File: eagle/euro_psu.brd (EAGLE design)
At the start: 99.4 x 50.2 mm, 40 parts, among them U1 POWER

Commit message: silkscreen draft
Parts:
- removed IC2: (no value), v-reg:317TS
- added LM317-2: (no value), v-reg:317TS
- added U2: POWER, eurorack:POWER_16
- moved PHASE1 17.8 mm to (21.6, 47.0)
- moved CT 13.7 mm to (16.5, 47.0)
- moved PHASE2 12.7 mm to (11.4, 47.0)
- moved U1 4.49 mm to (54.6, 44.5)
- moved C10 2.54 mm to (8.89, 11.4)
- moved C11 2.54 mm to (8.89, 29.2)
- moved C2 2.54 mm to (44.5, 11.4)
- moved C4 2.54 mm to (44.5, 29.2)
- moved C5 1.27 mm to (54.6, 3.81)
- moved D1 1.27 mm to (30.5, 43.2)
- moved D3 1.27 mm to (30.5, 38.1)
- moved C9 0.64 mm to (89.5, 27.9)
- renumbered +5_ADJ1 to +5_ADJ, -12_ADJ1 to -12_ADJ, IC1 to LM317-1, IC3 to LM337, LED1 to LED-12, LED2 to LED12, LED3 to LED5
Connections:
- net GNDA: now also U2.3, U2.4, U2.5, U2.6, U2.7, U2.8
- net N$10: now also U2.1, U2.2
- net N$11: now also LM317-2.2, U2.10, U2.9; no longer IC2.2
- net N$12: now also U2.11, U2.12
- net N$4: now also LM317-2.3; no longer IC2.3
- net N$6: now also LM317-2.1; no longer IC2.1
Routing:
- net N$12: track 51.9 -> 93.7 mm, vias 0 -> 1
- net N$11: track 138.9 -> 116.5 mm
- net N$1: track 39.7 -> 22.0 mm
- net GNDA: track 290.9 -> 307.9 mm
- net N$4: track 178.7 -> 186.2 mm, vias 1 -> 0
- net N$10: track 62.0 -> 56.9 mm, vias 1 -> 0
- net N$3: track 117.5 -> 121.6 mm
- net N$6: track 22.8 -> 25.8 mm
- net N$2: track 12.0 -> 10.4 mm
- net N$8: track 25.1 -> 24.2 mm
- net N$25: track 15.1 -> 14.5 mm
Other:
- board text added: "https://github.com/jbeuckm/euro_psu"
- board text removed: "https://github.com/jbeuckm/Roland-121-VCF"

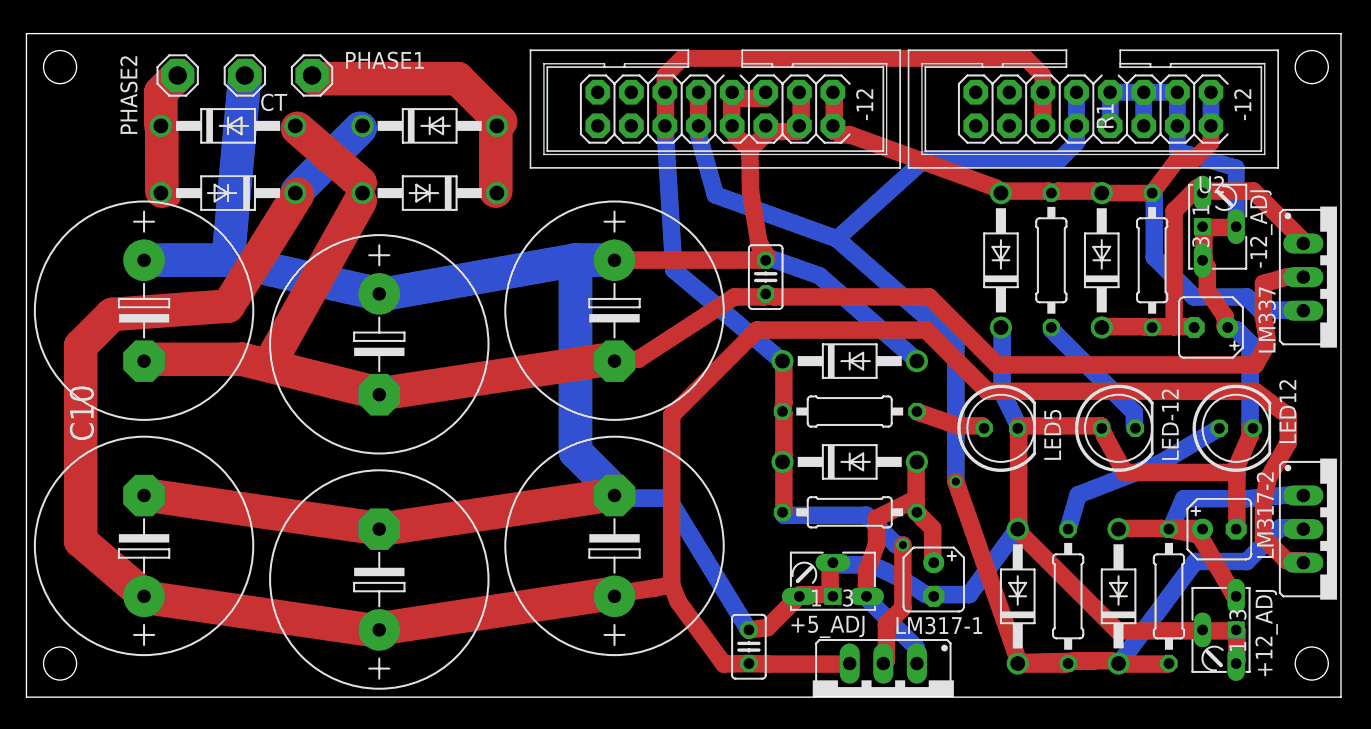
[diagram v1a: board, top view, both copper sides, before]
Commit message: rerouted with regulator protection diodes
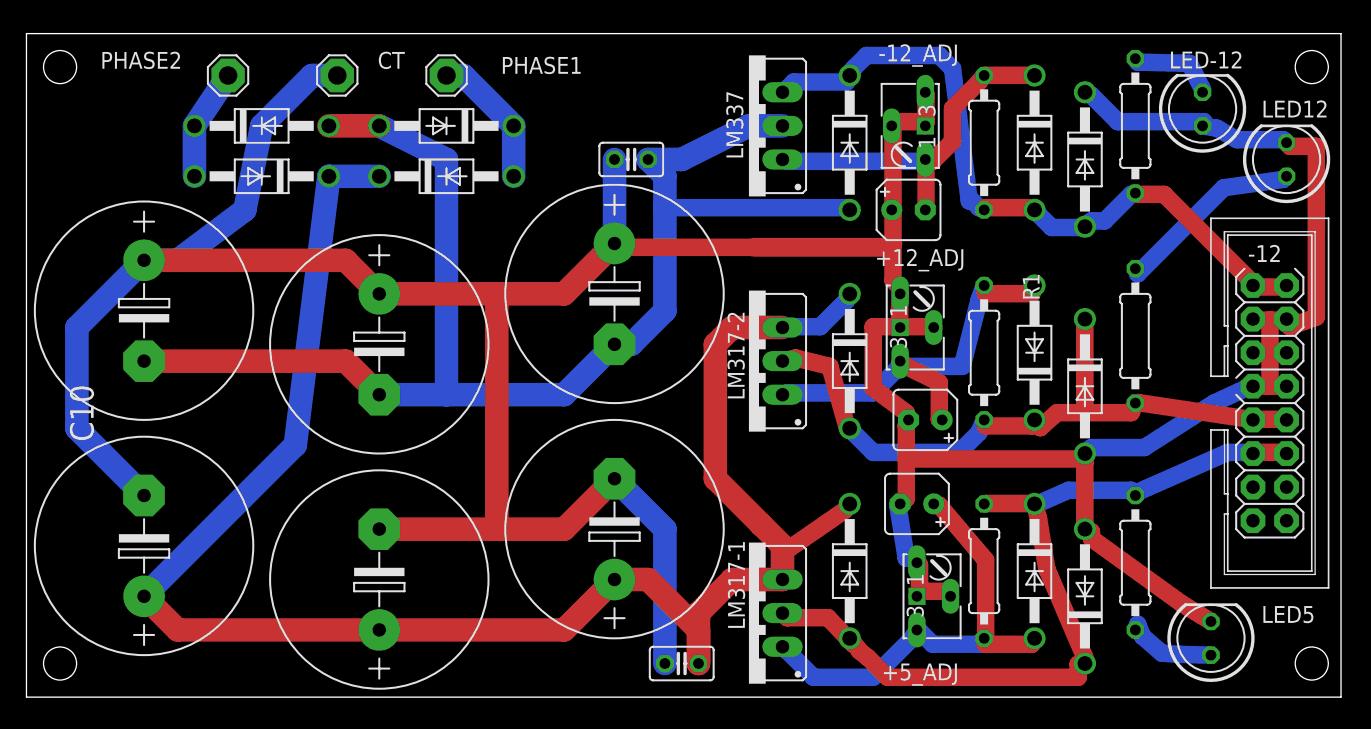
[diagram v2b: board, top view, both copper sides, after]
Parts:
- removed U2: POWER, eurorack:POWER_16
- added D11, D12, D13: 1N4004, diode:DO41-10
- R5, R6: value 4k7 -> 10k
- moved LM317-2 46.2 mm to (54.6, 25.4), turned to 90 degrees
- moved LM337 45.9 mm to (54.6, 43.2), turned to 90 degrees
- moved U1 44.0 mm to (94.0, 24.8), turned to 270 degrees
- moved +12_ADJ 34.2 mm to (66.0, 27.9), turned to 90 degrees
- moved D8 25.1 mm to (80.0, 7.62), turned to 90 degrees
- moved LED-12 25.0 mm to (88.9, 44.5), turned to 90 degrees
- moved C9 24.5 mm to (66.7, 36.8), turned to 0 degrees
- moved R4 24.4 mm to (83.8, 10.2), turned to 90 degrees
- moved C7 23.7 mm to (67.9, 21.0), turned to 180 degrees
- moved R2 23.1 mm to (72.4, 26.0)
- moved LED5 22.5 mm to (89.5, 4.45), turned to 90 degrees
- moved -12_ADJ 22.3 mm to (67.9, 43.2), turned to 270 degrees
- moved LED12 20.7 mm to (95.2, 40.6), turned to 90 degrees
- moved R5 20.3 mm to (83.8, 27.3)
- moved D6 19.5 mm to (76.2, 26.0)
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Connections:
- net GNDA: no longer U2.3, U2.4, U2.5, U2.6, U2.7, U2.8
- net N$10: now also D13.C; no longer U2.1, U2.2
- net N$11: now also D12.A; no longer U2.10, U2.9
- net N$12: now also D11.A; no longer U2.11, U2.12
- net N$3: now also D13.A
- net N$4: now also D11.C, D12.C
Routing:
- net N$11: track 116.5 -> 52.8 mm, vias 1 -> 0
- net N$4: track 186.2 -> 140.9 mm
- net N$12: track 93.7 -> 63.8 mm, vias 1 -> 0
- net N$3: track 121.6 -> 107.1 mm
- net N$1: track 22.0 -> 10.5 mm
- net N$8: track 24.2 -> 35.1 mm
- net N$6: track 25.8 -> 32.4 mm
- net N$24: track 10.2 -> 6.64 mm
- net N$10: track 56.9 -> 53.6 mm
- net N$2: track 10.4 -> 8.39 mm
- net N$21: track 5.36 -> 7.08 mm
- net N$5: track 28.3 -> 27.1 mm
- net GNDA: track 307.9 -> 307.2 mm

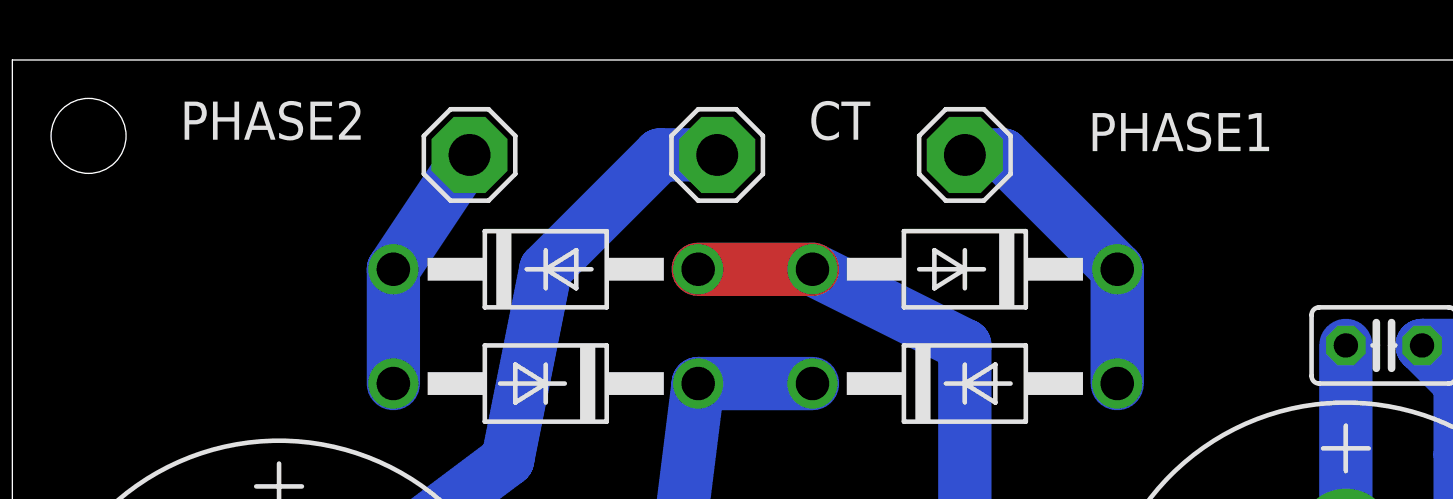
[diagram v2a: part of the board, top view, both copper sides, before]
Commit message: vector silkscreen
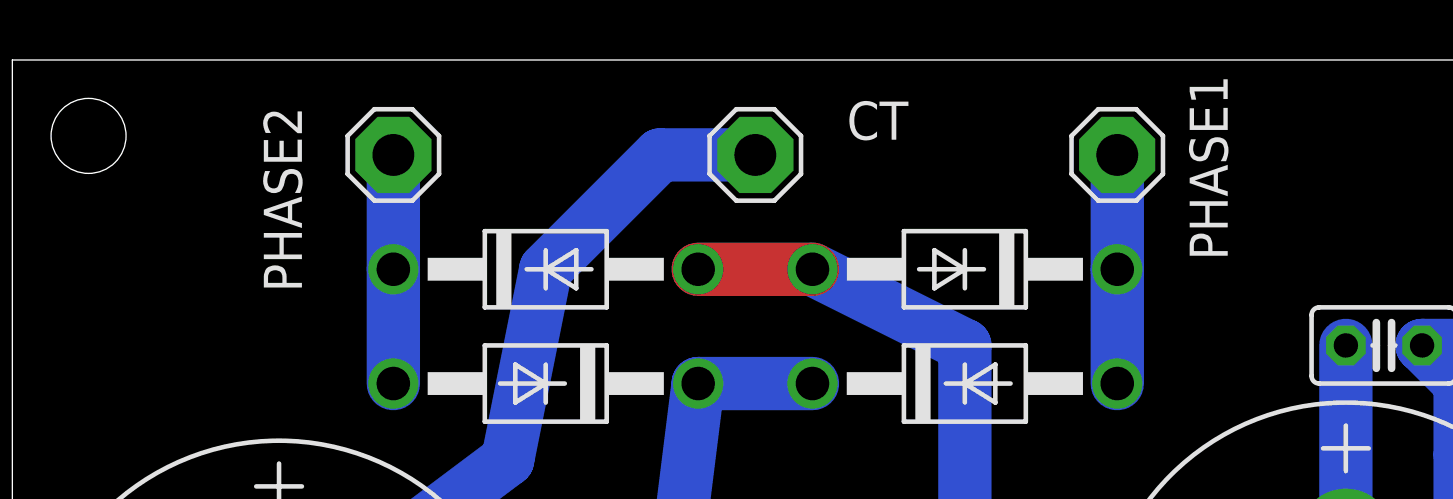
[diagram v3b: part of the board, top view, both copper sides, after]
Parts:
- moved PHASE1 5.08 mm to (36.8, 47.0)
- moved PHASE2 2.54 mm to (12.7, 47.0)
- moved CT 1.27 mm to (24.8, 47.0)
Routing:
- net N$1: track 10.5 -> 7.62 mm
- net GNDA: track 307.2 -> 308.5 mm
- net N$2: track 8.39 -> 7.62 mm
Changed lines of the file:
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@@
 <?xml version="1.0" encoding="utf-8"?>
 <!DOCTYPE eagle SYSTEM "eagle.dtd">
-<eagle version="7.6.0">
+<eagle version="8.3.2">
 <drawing>
 <settings>
 <setting alwaysvectorfont="no"/>
+<setting keepoldvectorfont="yes"/>
 <setting verticaltext="up"/>
 </settings>
@@
 <wire x1="99.365" y1="50.155" x2="0" y2="50.155" width="0" layer="20"/>
 <wire x1="0" y1="50.155" x2="0" y2="0" width="0" layer="20"/>
-<text x="53.975" y="19.05" size="2.1844" layer="26" rot="MR0">https://github.com/jbeuckm/euro_psu</text>
+<text x="59.055" y="17.78" size="2" layer="26" font="vector" rot="MR0">https://github.com/jbeuckm/euro_psu</text>
 <text x="52.07" y="22.225" size="2.1844" layer="26" rot="MR0">Release v0.1</text>
 <hole x="2.54" y="47.625" drill="2.5"/>
@@
 <element name="D3" library="diode" package="DO41-10" value="1N4004" x="31.75" y="43.18" smashed="yes" rot="R180"/>
 <element name="D4" library="diode" package="DO41-10" value="1N4004" x="17.78" y="43.18" smashed="yes"/>
-<element name="PHASE1" library="solpad" package="SE14" value="SE14" x="31.75" y="46.99" smashed="yes">
-<attribute name="NAME" x="42.037" y="48.387" size="1.27" layer="25" ratio="10" rot="R180"/>
-<attribute name="VALUE" x="31.75" y="47.371" size="0.0254" layer="27"/>
-</element>
-<element name="CT" library="solpad" package="SE14" value="SE14" x="23.495" y="46.99" smashed="yes">
-<attribute name="NAME" x="26.543" y="47.498" size="1.27" layer="25" ratio="10"/>
-<attribute name="VALUE" x="23.495" y="47.371" size="0.0254" layer="27"/>
-</element>
-<element name="PHASE2" library="solpad" package="SE14" value="SE14" x="15.24" y="46.99" smashed="yes">
-<attribute name="NAME" x="5.588" y="47.498" size="1.27" layer="25" ratio="10"/>
-<attribute name="VALUE" x="14.605" y="47.371" size="0.0254" layer="27"/>
+<element name="PHASE1" library="solpad" package="SE14" value="SE14" x="36.83" y="46.99" smashed="yes">
+<attribute name="NAME" x="39.243" y="49.657" size="1.27" layer="25" ratio="10" rot="R270"/>
+<attribute name="VALUE" x="36.83" y="47.371" size="0.0254" layer="27"/>
+</element>
+<element name="CT" library="solpad" package="SE14" value="SE14" x="24.765" y="46.99" smashed="yes">
+<attribute name="NAME" x="27.813" y="47.498" size="1.27" layer="25" ratio="10"/>
+<attribute name="VALUE" x="24.765" y="47.371" size="0.0254" layer="27"/>
+</element>
+<element name="PHASE2" library="solpad" package="SE14" value="SE14" x="12.7" y="46.99" smashed="yes">
+<attribute name="NAME" x="9.652" y="42.418" size="1.27" layer="25" ratio="10" rot="R90"/>
+<attribute name="VALUE" x="12.065" y="47.371" size="0.0254" layer="27"/>
 </element>
 <element name="C1" library="rcl" package="E7,5-16" value="3300uF" x="26.67" y="8.89" smashed="yes" rot="R90">
@@
 <contactref element="D1" pad="A"/>
 <contactref element="PHASE1" pad="MP"/>
-<wire x1="31.75" y1="46.99" x2="33.02" y2="46.99" width="1.778" layer="16"/>
 <wire x1="36.83" y1="43.18" x2="36.83" y2="39.37" width="1.778" layer="16"/>
-<wire x1="33.02" y1="46.99" x2="36.83" y2="43.18" width="1.778" layer="16"/>
+<wire x1="36.83" y1="46.99" x2="36.83" y2="43.18" width="1.778" layer="16"/>
 </signal>
 <signal name="N$2">
@@
 <contactref element="D4" pad="C"/>
 <contactref element="PHASE2" pad="MP"/>
-<wire x1="12.7" y1="43.18" x2="15.24" y2="46.99" width="1.778" layer="16"/>
+<wire x1="12.7" y1="43.18" x2="12.7" y2="46.99" width="1.778" layer="16"/>
 <wire x1="12.7" y1="43.18" x2="12.7" y2="39.37" width="1.778" layer="16"/>
 </signal>
@@
 <wire x1="16.51" y1="36.83" x2="17.78" y2="43.18" width="1.778" layer="16"/>
 <wire x1="17.78" y1="43.18" x2="21.59" y2="46.99" width="1.778" layer="16"/>
-<wire x1="21.59" y1="46.99" x2="23.495" y2="46.99" width="1.778" layer="16"/>
+<wire x1="21.59" y1="46.99" x2="24.765" y2="46.99" width="1.778" layer="16"/>
 <wire x1="8.89" y1="33.02" x2="24.13" y2="33.02" width="1.778" layer="1"/>
 <wire x1="24.13" y1="33.02" x2="26.67" y2="30.48" width="1.778" layer="1"/>

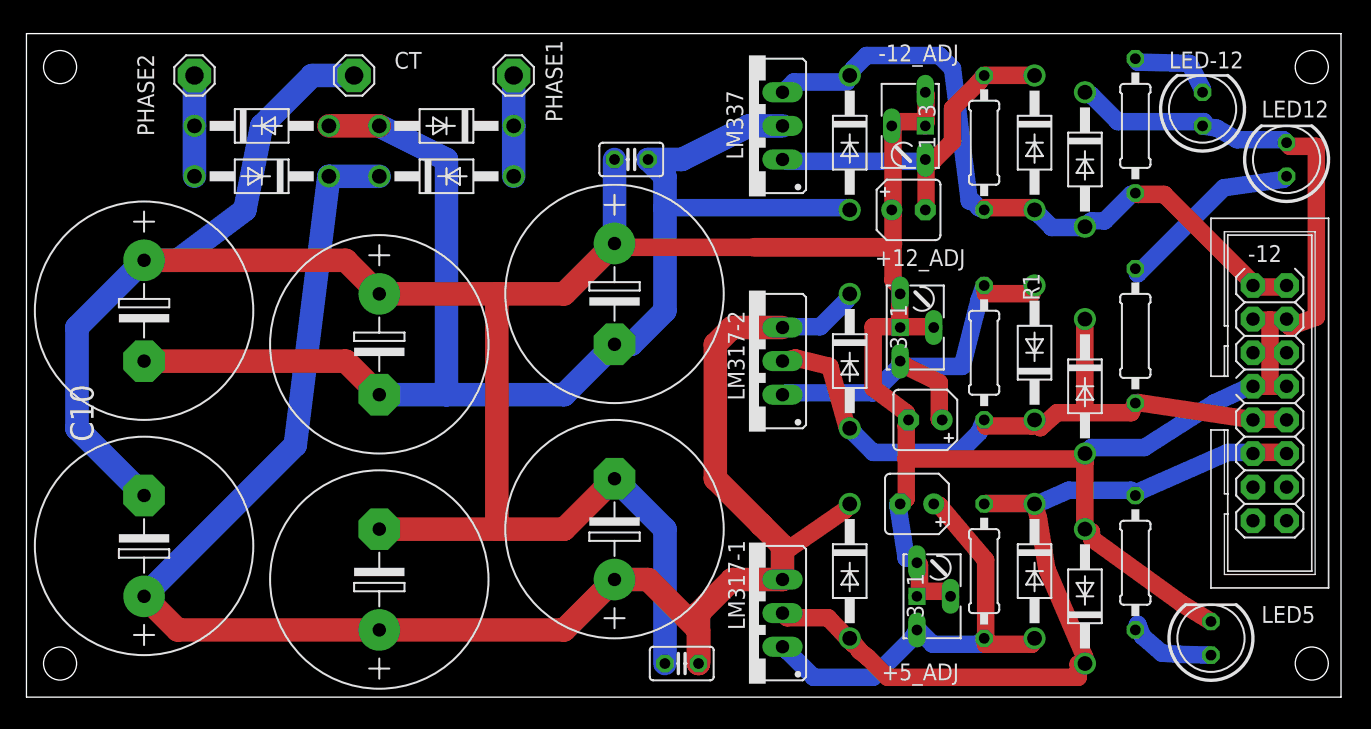
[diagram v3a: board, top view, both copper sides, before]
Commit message: tweaked for more space behind the regulators
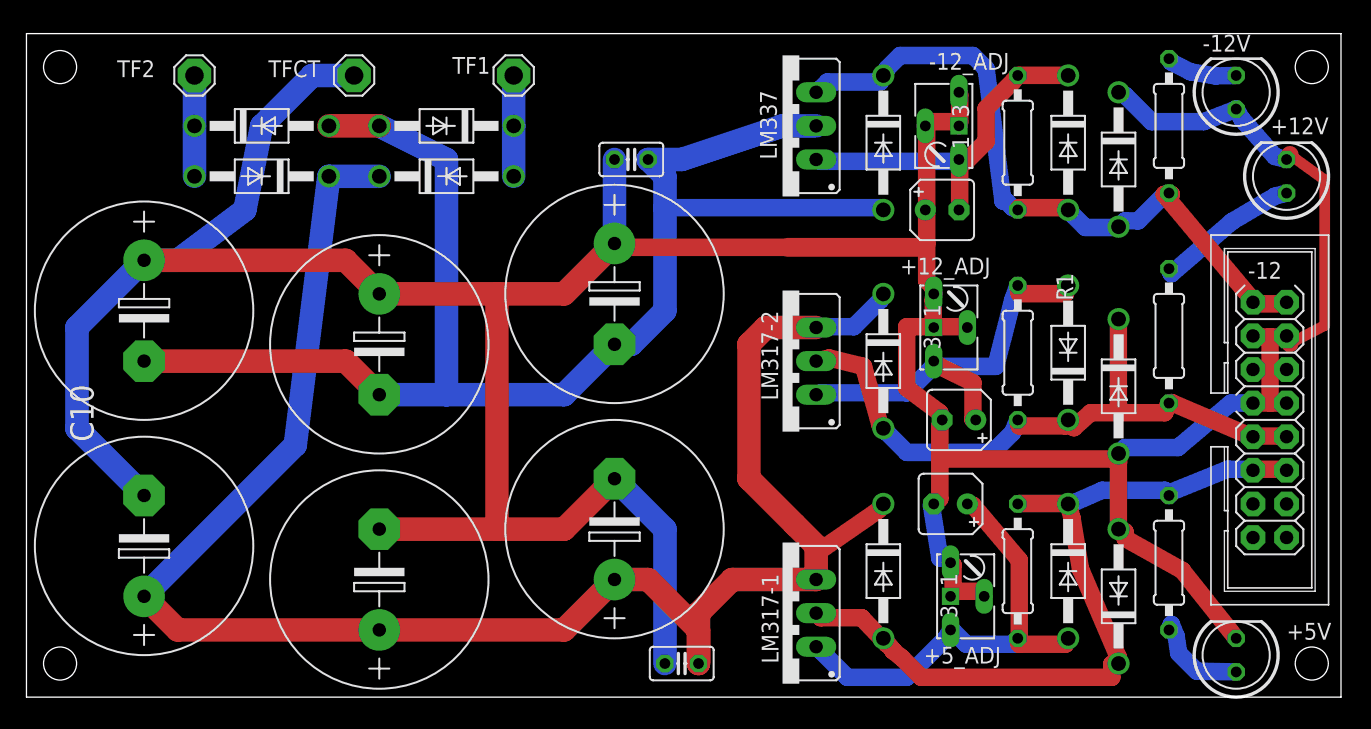
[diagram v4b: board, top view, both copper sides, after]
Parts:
- removed LED-12, LED12, LED5: (no value), led:LED5MM
- added +12V, +5V, -12V: (no value), led:LED5MM
- moved -12_ADJ 2.54 mm to (70.5, 43.2)
- moved C7 2.54 mm to (70.5, 21.0)
- moved C9 2.54 mm to (69.2, 36.8)
- moved R1 2.54 mm to (74.9, 41.9)
- moved R2 2.54 mm to (74.9, 26.0)
- moved R3 2.54 mm to (74.9, 9.53)
- moved R4 2.54 mm to (86.4, 10.2)
- moved R5 2.54 mm to (86.4, 27.3)
- moved R6 2.54 mm to (86.4, 43.2)
- moved D11 2.54 mm to (64.8, 9.53)
- moved D12 2.54 mm to (64.8, 25.4)
- moved D13 2.54 mm to (64.8, 41.9)
- moved LM317-1 2.54 mm to (57.1, 6.35)
- moved LM317-2 2.54 mm to (57.1, 25.4)
- moved LM337 2.54 mm to (57.1, 43.2)
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- renumbered CT to TFCT, PHASE1 to TF1, PHASE2 to TF2
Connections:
- net GNDA: now also +12V.K, +5V.K, -12V.A; no longer LED-12.A, LED12.K, LED5.K
- net N$21: now also +5V.A; no longer LED5.A
- net N$24: now also -12V.K; no longer LED-12.K
- net N$25: now also +12V.A; no longer LED12.A
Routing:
- net N$3: track 107.1 -> 112.0 mm
- net N$25: track 14.5 -> 11.2 mm
- net N$12: track 63.8 -> 61.0 mm
- net N$4: track 140.9 -> 143.5 mm
- net N$11: track 52.8 -> 50.6 mm
- net N$24: track 6.64 -> 5.42 mm
- net GNDA: track 308.5 -> 307.8 mm
- net N$21: track 7.08 -> 7.63 mm
- net N$10: track 53.6 -> 53.1 mm
